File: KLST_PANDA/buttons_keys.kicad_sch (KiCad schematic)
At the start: 0 parts

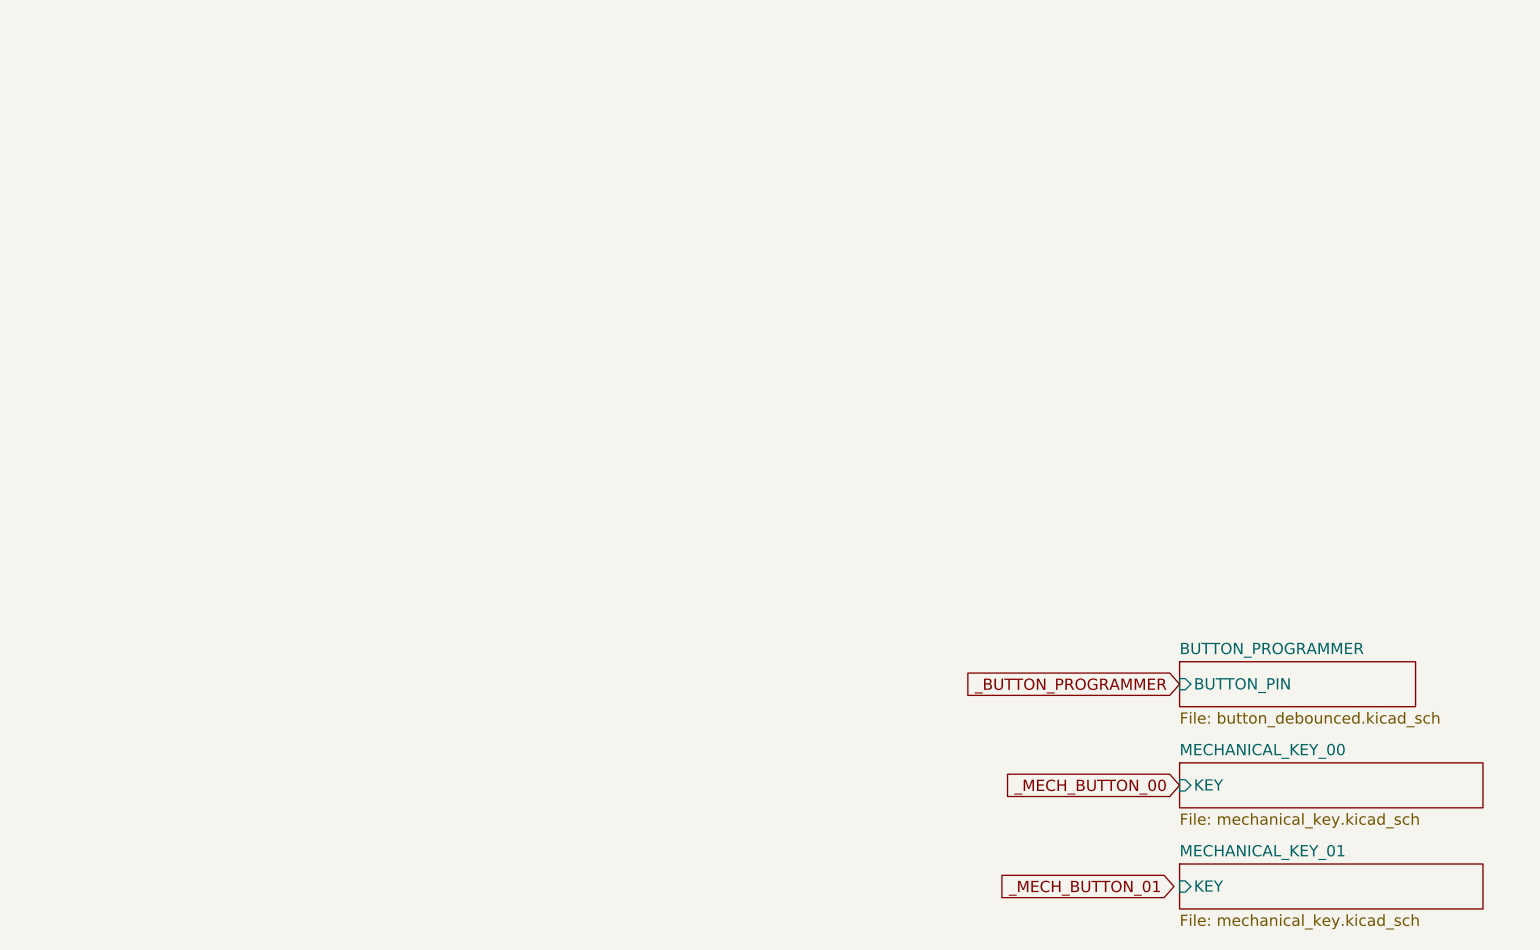
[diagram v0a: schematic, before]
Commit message: moved core (MCU) to sheet, cleaned up sheets
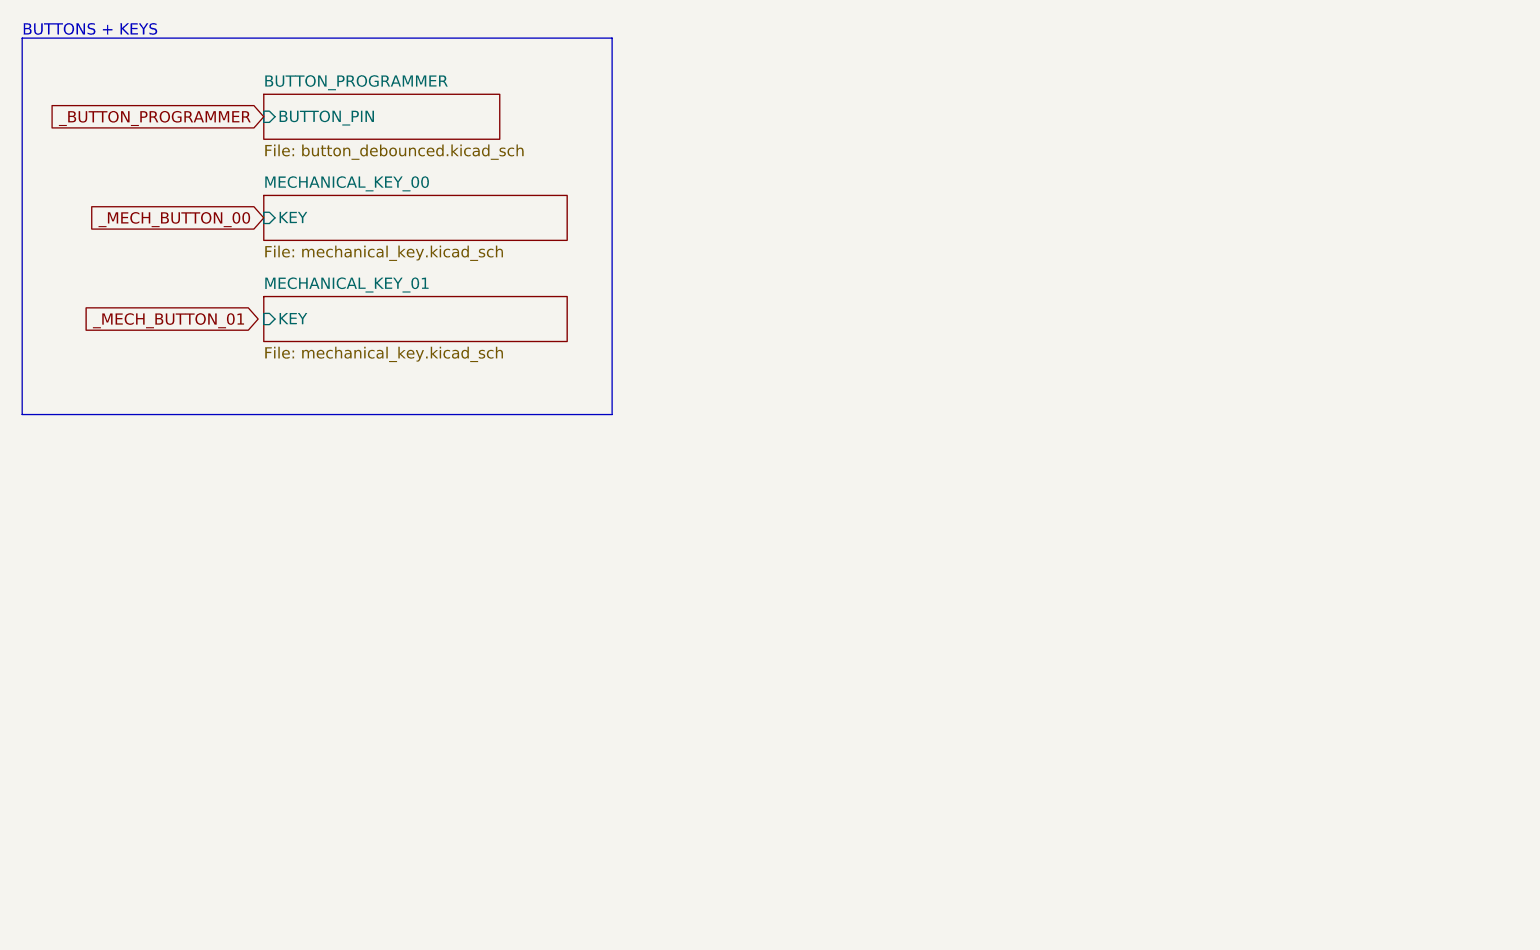
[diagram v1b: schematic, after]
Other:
- note added: "BUTTONS + KEYS"
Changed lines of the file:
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@@
 (kicad_sch (version 20230121) (generator eeschema)
   (paper "A4")
-  (global_label "_MECH_BUTTON_00" (shape input) (at 146.05 99.695 180) (fields_autoplaced)
+  (rectangle (start 15.24 15.24) (end 81.915 57.785)
+    (stroke (width 0) (type default))
+    (fill (type none))
+  )
+  (text "BUTTONS + KEYS" (at 15.24 15.24 0)
+    (effects (font (size 1.27 1.27)) (justify left bottom))
+  )
+  (global_label "_MECH_BUTTON_00" (shape input) (at 42.545 35.56 180) (fields_autoplaced)
     (effects (font (size 1.27 1.27)) (justify right))
-    (property "Intersheetrefs" "${INTERSHEET_REFS}" (at 125.4248 99.695 0)
+    (property "Intersheetrefs" "${INTERSHEET_REFS}" (at 21.9198 35.56 0)
       (effects (font (size 1.27 1.27)) (justify right) hide)
     )
   )
-  (global_label "_MECH_BUTTON_01" (shape input) (at 145.415 111.125 180) (fields_autoplaced)
+  (global_label "_MECH_BUTTON_01" (shape input) (at 41.91 46.99 180) (fields_autoplaced)
     (effects (font (size 1.27 1.27)) (justify right))
-    (property "Intersheetrefs" "${INTERSHEET_REFS}" (at 124.7898 111.125 0)
+    (property "Intersheetrefs" "${INTERSHEET_REFS}" (at 21.2848 46.99 0)
       (effects (font (size 1.27 1.27)) (justify right) hide)
     )
   )
-  (global_label "_BUTTON_PROGRAMMER" (shape input) (at 146.05 88.265 180) (fields_autoplaced)
+  (global_label "_BUTTON_PROGRAMMER" (shape input) (at 42.545 24.13 180) (fields_autoplaced)
     (effects (font (size 1.27 1.27)) (justify right))
-    (property "Intersheetrefs" "${INTERSHEET_REFS}" (at 121.1914 88.265 0)
+    (property "Intersheetrefs" "${INTERSHEET_REFS}" (at 17.6864 24.13 0)
       (effects (font (size 1.27 1.27)) (justify right) hide)
     )
   )
-  (sheet (at 146.05 97.155) (size 34.29 5.08) (fields_autoplaced)
+  (sheet (at 42.545 33.02) (size 34.29 5.08) (fields_autoplaced)
     (stroke (width 0.1524) (type solid))
     (fill (color 0 0 0 0.0000))
-    (property "Sheetname" "MECHANICAL_KEY_00" (at 146.05 96.4434 0)
+    (property "Sheetname" "MECHANICAL_KEY_00" (at 42.545 32.3084 0)
       (effects (font (size 1.27 1.27)) (justify left bottom))
     )
-    (property "Sheetfile" "mechanical_key.kicad_sch" (at 146.05 102.8196 0)
+    (property "Sheetfile" "mechanical_key.kicad_sch" (at 42.545 38.6846 0)
       (effects (font (size 1.27 1.27)) (justify left top))
     )
-    (pin "KEY" input (at 146.05 99.695 180)
+    (pin "KEY" input (at 42.545 35.56 180)
       (effects (font (size 1.27 1.27)) (justify left))
     )
@@
     )
   )
-  (sheet (at 146.05 85.725) (size 26.67 5.08) (fields_autoplaced)
+  (sheet (at 42.545 21.59) (size 26.67 5.08) (fields_autoplaced)
     (stroke (width 0.1524) (type solid))
     (fill (color 0 0 0 0.0000))
-    (property "Sheetname" "BUTTON_PROGRAMMER" (at 146.05 85.0134 0)
+    (property "Sheetname" "BUTTON_PROGRAMMER" (at 42.545 20.8784 0)
       (effects (font (size 1.27 1.27)) (justify left bottom))
     )
-    (property "Sheetfile" "button_debounced.kicad_sch" (at 146.05 91.3896 0)
+    (property "Sheetfile" "button_debounced.kicad_sch" (at 42.545 27.2546 0)
       (effects (font (size 1.27 1.27)) (justify left top))
     )
-    (pin "BUTTON_PIN" input (at 146.05 88.265 180)
+    (pin "BUTTON_PIN" input (at 42.545 24.13 180)
       (effects (font (size 1.27 1.27)) (justify left))
     )
@@
     )
   )
-  (sheet (at 146.05 108.585) (size 34.29 5.08) (fields_autoplaced)
+  (sheet (at 42.545 44.45) (size 34.29 5.08) (fields_autoplaced)
     (stroke (width 0.1524) (type solid))
     (fill (color 0 0 0 0.0000))
-    (property "Sheetname" "MECHANICAL_KEY_01" (at 146.05 107.8734 0)
+    (property "Sheetname" "MECHANICAL_KEY_01" (at 42.545 43.7384 0)
       (effects (font (size 1.27 1.27)) (justify left bottom))
     )
-    (property "Sheetfile" "mechanical_key.kicad_sch" (at 146.05 114.2496 0)
+    (property "Sheetfile" "mechanical_key.kicad_sch" (at 42.545 50.1146 0)
       (effects (font (size 1.27 1.27)) (justify left top))
     )
-    (pin "KEY" input (at 146.05 111.125 180)
+    (pin "KEY" input (at 42.545 46.99 180)
       (effects (font (size 1.27 1.27)) (justify left))
     )

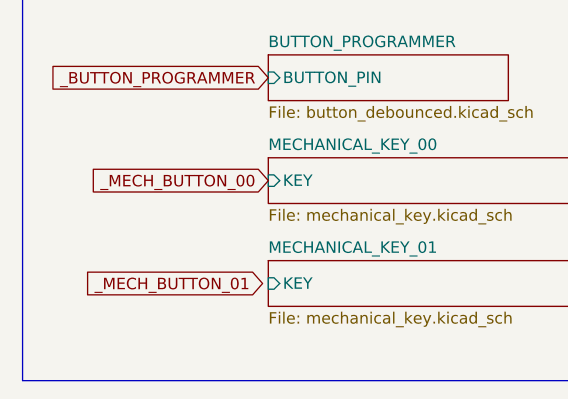
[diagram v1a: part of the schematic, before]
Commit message: started cleaning up schematic ( addressing DRC errors/warning ) (WIP)
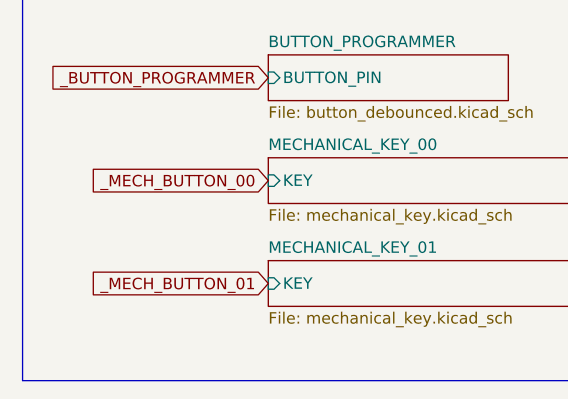
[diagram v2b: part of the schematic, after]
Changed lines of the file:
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@@
     )
   )
-  (global_label "_MECH_BUTTON_01" (shape input) (at 41.91 46.99 180) (fields_autoplaced)
+  (global_label "_MECH_BUTTON_01" (shape input) (at 42.545 46.99 180) (fields_autoplaced)
     (effects (font (size 1.27 1.27)) (justify right))
-    (property "Intersheetrefs" "${INTERSHEET_REFS}" (at 21.2848 46.99 0)
+    (property "Intersheetrefs" "${INTERSHEET_REFS}" (at 21.9198 46.99 0)
       (effects (font (size 1.27 1.27)) (justify right) hide)
     )
